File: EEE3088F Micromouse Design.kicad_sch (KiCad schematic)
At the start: 95 parts, among them J1 Conn_02x16_Odd_Even, J2 Conn_01x02, J3 TYPE-C-31-M-12, Q2 AO3400A, SW1 SW_SPDT, U1 INA219AxD, U11 DRV8833PW, U12 DRV8833PW, U13 AP22966DC8-7, U14 XL1509-5.0, U15 TP4056-42-ESOP8, U2 XL1509-3.3, U7 TPS61088RHLR, U9 CH224K

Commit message: Fixed the arc to match spec. Added Daniel's components and added all LCSC numbers for them. Fixed the connector footprint, although JST one still needs to be corrected
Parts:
- C16, C17: LCSC (none) -> C1525
- C18: LCSC (none) -> C1622
- C19: LCSC (none) -> C1588
- C20, C21, C22: LCSC (none) -> C12891
- C24: LCSC (none) -> C52923
- C39: LCSC (none) -> C15850
- J3: LCSC (none) -> C165948
- L2: LCSC (none) -> C167204
- R15: LCSC (none) -> C11702
- R16: LCSC (none) -> C17772
- R18: LCSC (none) -> C17414
- R21: LCSC (none) -> C4216
- R4: LCSC (none) -> C17556
- R5: LCSC (none) -> C17900
- R6: LCSC (none) -> C17801
- R7: LCSC (none) -> C17713
- R8: LCSC (none) -> C17470
- U2: LCSC (none) -> C61063
- U7: footprint TPS61088RHLR:IC_TPS61088RHLR -> TPS61088:IC_TPS61088RHLR; LCSC (none) -> C87357
- U9: LCSC (none) -> C970725

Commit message: Found the correct Battery connector
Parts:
- J2: footprint Connector_JST:JST_JWPF_B02B-JWPF-SK-R_1x02_P2.00mm_Vertical -> Connector_JST:JST_PH_B2B-PH-K_1x02_P2.00mm_Vertical
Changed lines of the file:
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@@
 		(exclude_from_sim no)
 		(in_bom yes)
-		(on_board yes)
+		(on_board no)
 		(dnp no)
 		(property "Reference" "C26"
@@
 		(exclude_from_sim no)
 		(in_bom yes)
-		(on_board yes)
+		(on_board no)
 		(dnp no)
 		(fields_autoplaced yes)
@@
 		(exclude_from_sim no)
 		(in_bom yes)
-		(on_board yes)
+		(on_board no)
 		(dnp no)
 		(property "Reference" "C29"
@@
 		(exclude_from_sim no)
 		(in_bom yes)
-		(on_board yes)
+		(on_board no)
 		(dnp no)
 		(fields_autoplaced yes)
@@
 		(exclude_from_sim no)
 		(in_bom yes)
-		(on_board yes)
+		(on_board no)
 		(dnp no)
 		(property "Reference" "C30"
@@
 		(exclude_from_sim no)
 		(in_bom yes)
-		(on_board yes)
+		(on_board no)
 		(dnp no)
 		(fields_autoplaced yes)
@@
 		(exclude_from_sim no)
 		(in_bom yes)
-		(on_board yes)
+		(on_board no)
 		(dnp no)
 		(fields_autoplaced yes)
@@
 		(exclude_from_sim no)
 		(in_bom yes)
-		(on_board yes)
+		(on_board no)
 		(dnp no)
 		(property "Reference" "C31"
@@
 		(exclude_from_sim no)
 		(in_bom yes)
-		(on_board yes)
+		(on_board no)
 		(dnp no)
 		(property "Reference" "C38"
@@
 		(exclude_from_sim no)
 		(in_bom yes)
-		(on_board yes)
+		(on_board no)
 		(dnp no)
 		(fields_autoplaced yes)
@@
 		(exclude_from_sim no)
 		(in_bom yes)
-		(on_board yes)
+		(on_board no)
 		(dnp no)
 		(fields_autoplaced yes)
@@
 		(exclude_from_sim no)
 		(in_bom yes)
-		(on_board yes)
+		(on_board no)
 		(dnp no)
 		(fields_autoplaced yes)
@@
 		(exclude_from_sim no)
 		(in_bom yes)
-		(on_board yes)
+		(on_board no)
 		(dnp no)
 		(property "Reference" "R25"
@@
 		(exclude_from_sim no)
 		(in_bom yes)
-		(on_board yes)
+		(on_board no)
 		(dnp no)
 		(fields_autoplaced yes)
@@
 		(exclude_from_sim no)
 		(in_bom yes)
-		(on_board yes)
+		(on_board no)
 		(dnp no)
 		(fields_autoplaced yes)
@@
 		(exclude_from_sim no)
 		(in_bom yes)
-		(on_board yes)
+		(on_board no)
 		(dnp no)
 		(fields_autoplaced yes)
@@
 		(exclude_from_sim no)
 		(in_bom yes)
-		(on_board yes)
+		(on_board no)
 		(dnp no)
 		(fields_autoplaced yes)
@@
 			)
 		)
-		(property "Footprint" "Connector_JST:JST_JWPF_B02B-JWPF-SK-R_1x02_P2.00mm_Vertical"
+		(property "Footprint" "Connector_JST:JST_PH_B2B-PH-K_1x02_P2.00mm_Vertical"
 			(at 54.61 32.385 0)
 			(effects
@@
 		(exclude_from_sim no)
 		(in_bom yes)
-		(on_board yes)
+		(on_board no)
 		(dnp no)
 		(fields_autoplaced yes)
@@
 		(exclude_from_sim no)
 		(in_bom yes)
-		(on_board yes)
+		(on_board no)
 		(dnp no)
 		(fields_autoplaced yes)
@@
 		(exclude_from_sim no)
 		(in_bom yes)
-		(on_board yes)
+		(on_board no)
 		(dnp no)
 		(fields_autoplaced yes)
@@
 		(exclude_from_sim no)
 		(in_bom yes)
-		(on_board yes)
+		(on_board no)
 		(dnp no)
 		(property "Reference" "R26"
@@
 		(exclude_from_sim no)
 		(in_bom yes)
-		(on_board yes)
+		(on_board no)
 		(dnp no)
 		(property "Reference" "C28"
@@
 		(exclude_from_sim no)
 		(in_bom yes)
-		(on_board yes)
+		(on_board no)
 		(dnp no)
 		(fields_autoplaced yes)
@@
 		(exclude_from_sim no)
 		(in_bom yes)
-		(on_board yes)
+		(on_board no)
 		(dnp no)
 		(fields_autoplaced yes)
@@
 		(exclude_from_sim no)
 		(in_bom yes)
-		(on_board yes)
+		(on_board no)
 		(dnp no)
 		(fields_autoplaced yes)
@@
 		(exclude_from_sim no)
 		(in_bom yes)
-		(on_board yes)
+		(on_board no)
 		(dnp no)
 		(fields_autoplaced yes)
@@
 		(exclude_from_sim no)
 		(in_bom yes)
-		(on_board yes)
+		(on_board no)
 		(dnp no)
 		(fields_autoplaced yes)
@@
 		(exclude_from_sim no)
 		(in_bom yes)
-		(on_board yes)
+		(on_board no)
 		(dnp no)
 		(fields_autoplaced yes)
@@
 		(exclude_from_sim no)
 		(in_bom yes)
-		(on_board yes)
+		(on_board no)
 		(dnp no)
 		(fields_autoplaced yes)
@@
 		(exclude_from_sim no)
 		(in_bom yes)
-		(on_board yes)
+		(on_board no)
 		(dnp no)
 		(fields_autoplaced yes)

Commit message: Added test points and an inductor that was not populated. Added labels
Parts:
- removed TP1, TP3, TP5, TP7: TestPoint, TestPoint:TestPoint_Pad_D2.0mm, symbol Connector:TestPoint
- added TP16, TP17, TP20, TP21, TP22, TP23, Testpoint1: TestPoint, TestPoint:TestPoint_Pad_D2.0mm, symbol Connector:TestPoint
- L1: footprint (none) -> Inductor_SMD:L_0603_1608Metric_Pad1.05x0.95mm_HandSolder; LCSC (none) -> C1026
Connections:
- net 3.3V Out: now also TP16.1
- net 5V Out: now also TP17.1
- net GND: now also U1.2 (A0)
- net HV: now also TP23.1
- net V_Battery+: now also Testpoint1.1
- net V_Battery-: no longer U1.2 (A0)
- net Vcc: now also TP21.1
- net at C17.2, L2.2, R21.1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: now also TP22.1
- net at R6.2, U7.18 (COMP): now also TP20.1

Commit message: Found a component that I had not footprinted yet. use the footprint list to check yours please
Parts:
- C1: footprint (none) -> Capacitor_SMD:C_0402_1005Metric_Pad0.74x0.62mm_HandSolder; LCSC (none) -> C52923
- R6: LCSC C17801 -> C17801
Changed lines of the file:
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@@
 			)
 		)
-		(property "LCSC" "     C17801"
+		(property "LCSC" "C17801"
 			(at 447.04 63.5 90)
 			(effects
@@
 			)
 		)
-		(property "Footprint" ""
+		(property "Footprint" "Capacitor_SMD:C_0402_1005Metric_Pad0.74x0.62mm_HandSolder"
 			(at 246.38 43.18 0)
 			(effects
@@
 			(at 246.38 43.18 0)
 			(effects
+				(font
+					(size 1.27 1.27)
+				)
+				(hide yes)
+			)
+		)
+		(property "LCSC" "C52923"
+			(at 246.38 43.18 0)
+			(effects

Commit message: Added a bunch of changes
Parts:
- removed C2, C4, C5, C6: 100uF, Capacitor_SMD:C_1206_3216Metric_Pad1.33x1.80mm_HandSolder, symbol Device:C_Small
- removed C7: 47uF, Capacitor_SMD:C_1206_3216Metric_Pad1.33x1.80mm_HandSolder, symbol Device:C_Small
- removed D1: 1N5819, Diode_THT:D_DO-41_SOD81_P10.16mm_Horizontal, symbol Diode:1N5819
- removed R25: 1, Resistor_SMD:R_1206_3216Metric_Pad1.30x1.75mm_HandSolder, symbol Device:R_Small_US
- removed R3, R9: 2, Resistor_SMD:R_2512_6332Metric_Pad1.40x3.35mm_HandSolder, symbol Device:R_Small_US
- removed TP9: TestPoint, TestPoint:TestPoint_Pad_D2.0mm, symbol Connector:TestPoint
- added C41, C44, C45: 10uF, Capacitor_SMD:C_0805_2012Metric_Pad1.18x1.45mm_HandSolder, symbol Device:C_Small
- added C46, C48, C49, C50: 100uF, Capacitor_Tantalum_SMD:CP_EIA-3528-21_Kemet-B, symbol Device:C_Small
- added C47: 47uF, Capacitor_SMD:C_1206_3216Metric_Pad1.33x1.80mm_HandSolder, symbol Device:C_Small
- added D4: SS32, Diode_SMD:D_SMA, symbol Diode:SS32
- added R35: 1, Resistor_SMD:R_1206_3216Metric_Pad1.30x1.75mm_HandSolder, symbol Device:R_Small_US
- C12, C13, C23, C25: footprint Capacitor_SMD:C_1206_3216Metric_Pad1.33x1.80mm_HandSolder -> Capacitor_Tantalum_SMD:CP_EIA-3528-21_Kemet-B; LCSC C27279 -> C7196
- C26, C38: value 10uF -> 100uF; footprint Capacitor_SMD:C_0805_2012Metric_Pad1.18x1.45mm_HandSolder -> Capacitor_Tantalum_SMD:CP_EIA-3528-21_Kemet-B; LCSC (none) -> C7196
- C27: value 10uF -> 1uF; footprint Capacitor_SMD:C_0805_2012Metric_Pad1.18x1.45mm_HandSolder -> Capacitor_SMD:C_0402_1005Metric_Pad0.74x0.62mm_HandSolder; LCSC (none) -> C52923
- C28, C30: footprint Capacitor_SMD:C_0402_1005Metric -> Capacitor_SMD:C_0603_1608Metric; LCSC (none) -> C57112
- C29, C31: footprint Capacitor_SMD:C_0402_1005Metric -> Capacitor_SMD:C_0603_1608Metric_Pad1.08x0.95mm_HandSolder; LCSC (none) -> C23630
- C32, C33, C34: LCSC (none) -> C52923
- C35: value 1uF -> 1nF; footprint Capacitor_SMD:C_0402_1005Metric_Pad0.74x0.62mm_HandSolder -> Capacitor_SMD:C_0603_1608Metric; LCSC (none) -> C1588
- C36: LCSC (none) -> C1588
- C37: value 1nF -> 100uF; footprint Capacitor_SMD:C_0603_1608Metric -> Capacitor_Tantalum_SMD:CP_EIA-3528-21_Kemet-B; LCSC (none) -> C7196
- C40: value 100μF -> 100uF; footprint Capacitor_SMD:C_1206_3216Metric_Pad1.33x1.80mm_HandSolder -> Capacitor_Tantalum_SMD:CP_EIA-3528-21_Kemet-B; LCSC (none) -> C7196
- D3: LCSC (none) -> C34897
- Q2: LCSC (none) -> C20917
- R19: LCSC (none) -> C17414
- R26: LCSC (none) -> C17928
- R27: LCSC (none) -> C17936
- R28: LCSC (none) -> C17630
- R29, R30, R31, R32: LCSC (none) -> C3013351
- R33: LCSC (none) -> C4190
- R34: LCSC (none) -> C22966
- U13: LCSC (none) -> C441830
- U14: LCSC (none) -> C61063
- U15: LCSC (none) -> C7473158
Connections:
- net 5V Out: now also C27.1, C32.2, C37.1, C38.1, C40.1, C46.1, C47.1; no longer C32.1, C33.2
- net EXT_LOAD1_OUT: now also C33.1; no longer C34.1
- net EXT_LOAD2_OUT: now also C34.2; no longer C35.2
- net GND: now also C32.1, C33.2, C34.1, C35.2, C38.2, C40.2, C41.1, C44.2, C45.1, C46.2, C47.2, C48.1, C49.1, C50.1, D4.2 (A), R35.2; no longer C32.2, C33.1, C34.2, C35.1, C38.1, C40.1
- net HV: now also C26.2, C48.2, C49.2, C50.2; no longer C40.2
- net V_Battery+: now also C41.2, C44.1, C45.2; no longer C26.2, C27.1, C38.2
- net at TP4.1, U11.3 (AISEN): now also R35.1
- net at L1.1, U2.2 (OUT): now also D4.1 (K)
- net at U13.10 (SS2): now also C36.1; no longer C37.1
- net at U13.12 (SS1): now also C35.1; no longer C36.1
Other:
- note added: "Changes: - Replaced 1N5819 with SS32"
- note removed: "5V Battey Charger"
- moved on the sheet: C12, C14, C15, D3, L3, L4, L5, U14

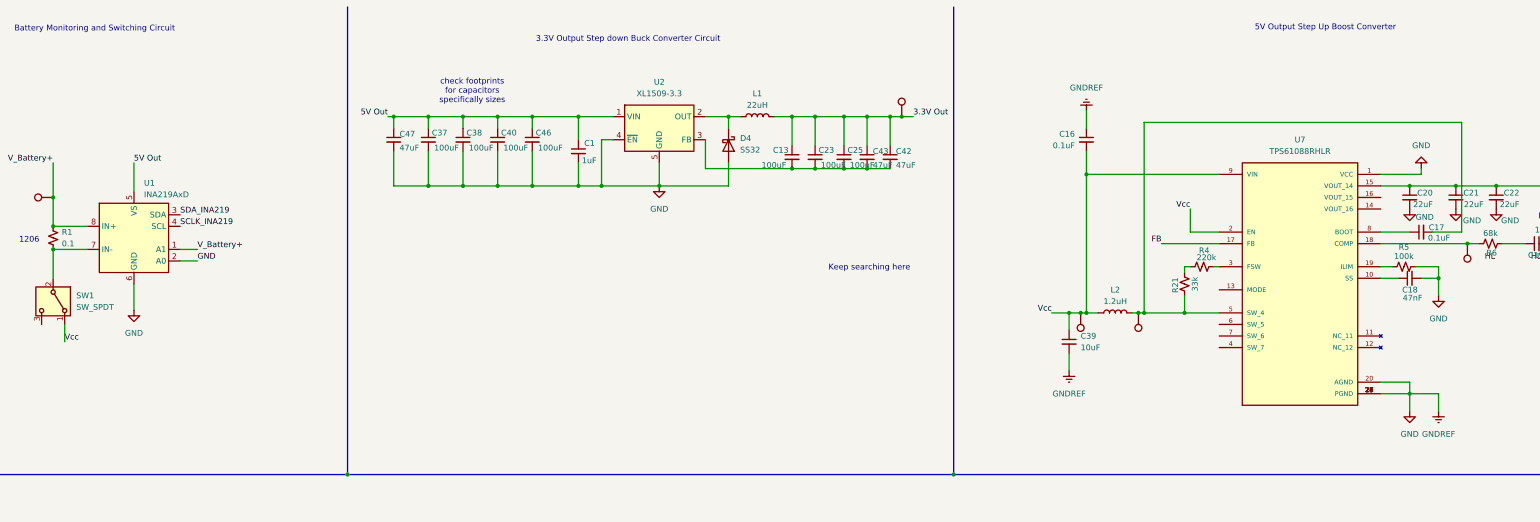
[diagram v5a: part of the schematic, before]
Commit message: Updated the INA219 circuit
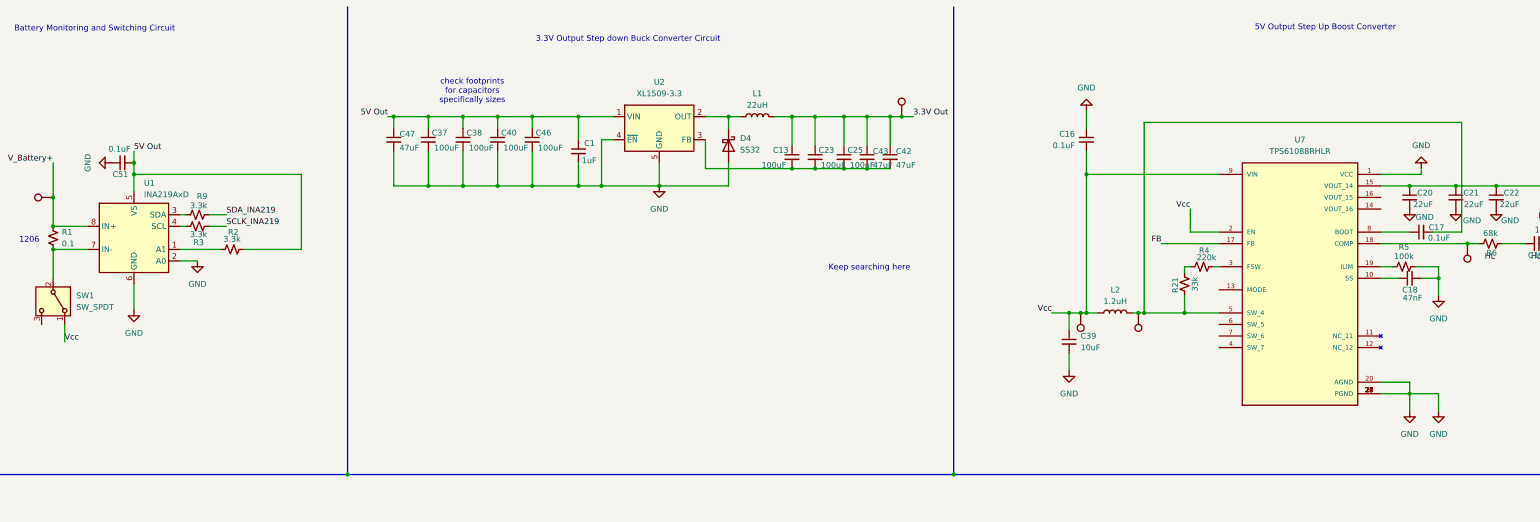
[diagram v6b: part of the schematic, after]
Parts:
- added C51: 0.1uF, Capacitor_SMD:C_0402_1005Metric_Pad0.74x0.62mm_HandSolder, symbol Device:C_Small
- added R2, R3, R9: 3.3k, Resistor_SMD:R_0402_1005Metric_Pad0.72x0.64mm_HandSolder, symbol Device:R_Small_US
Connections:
- net 5V Out: now also C51.2, R2.2
- net GND: now also C51.1
- net SCLK_INA219: now also R3.2; no longer U1.4 (SCL)
- net SDA_INA219: now also R9.2; no longer U1.3 (SDA)
- net V_Battery+: no longer U1.1 (A1)
- new net: R9.1, U1.3 (SDA)
- new net: R2.1, U1.1 (A1)
- new net: R3.1, U1.4 (SCL)

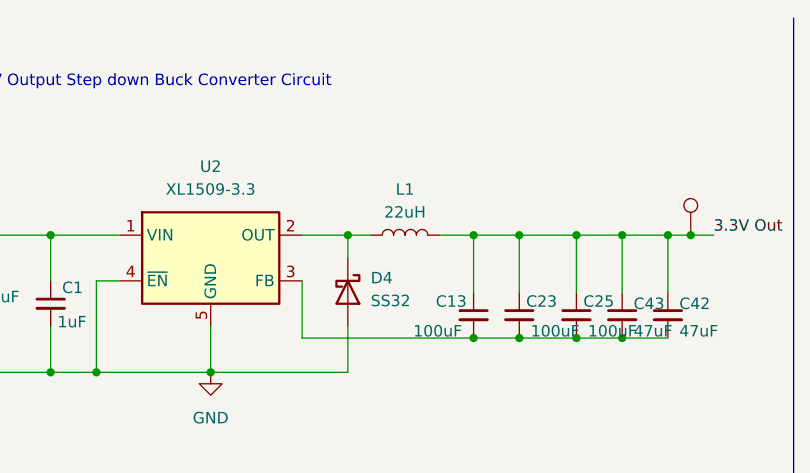
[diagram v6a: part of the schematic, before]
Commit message: First turnover, changed pcb layout
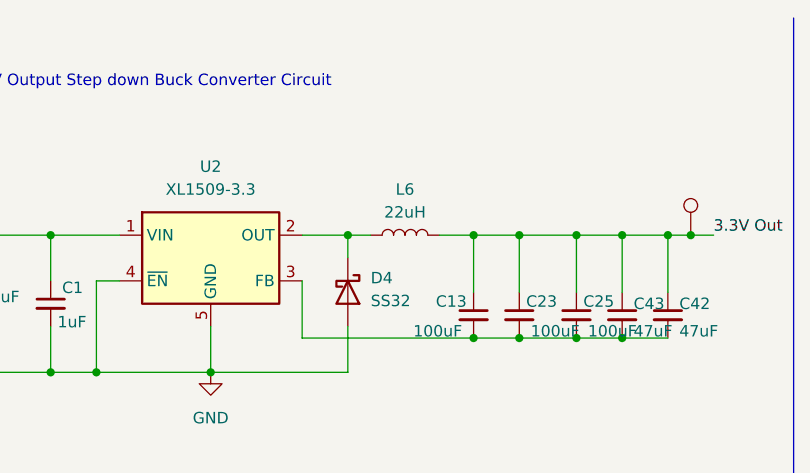
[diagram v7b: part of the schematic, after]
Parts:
- removed L1: 22uH, Inductor_SMD:L_0603_1608Metric_Pad1.05x0.95mm_HandSolder, symbol Device:L
- added L6: 22uH, Inductor_SMD:L_7.3x7.3_H4.5, symbol Device:L
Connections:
- net 3.3V Out: now also L6.2
- net at D4.1 (K), U2.2 (OUT): now also L6.1
